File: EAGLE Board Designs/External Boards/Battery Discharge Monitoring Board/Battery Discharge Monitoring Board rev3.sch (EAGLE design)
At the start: 88 parts, among them Q1 LMMBT3904LT3G, Q2 LMMBT3904LT3G, Q3 LMMBT3904LT3G, Q4 LMMBT3904LT3G

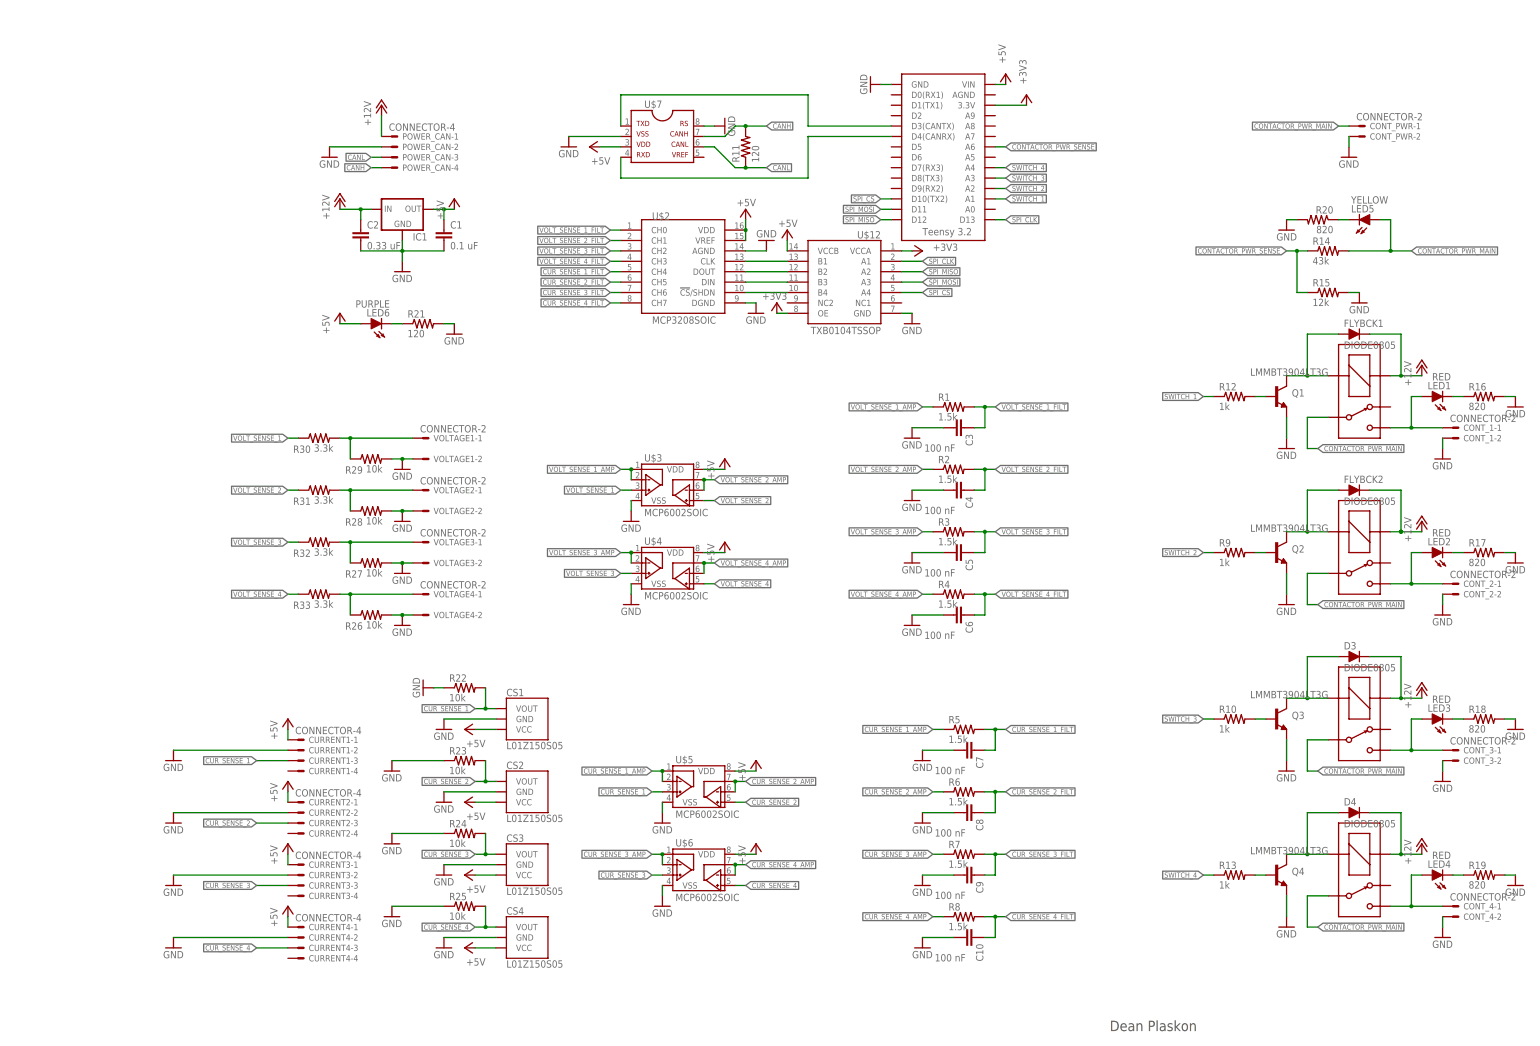
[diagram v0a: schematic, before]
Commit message: updated battery discharge monitoring rev3
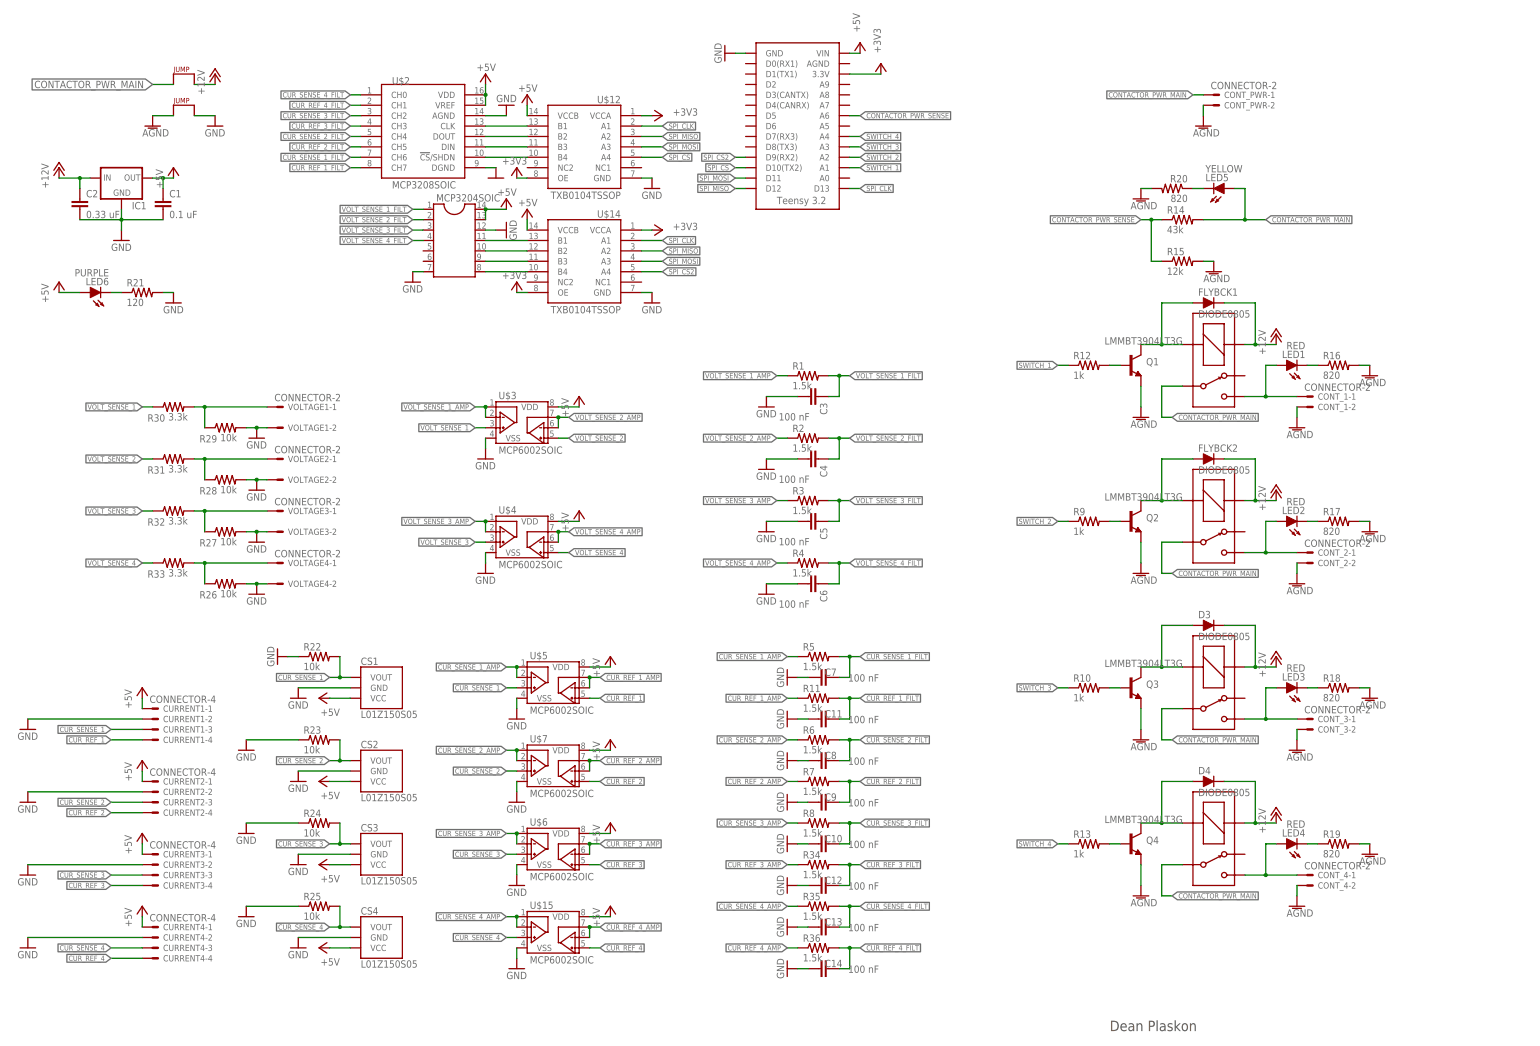
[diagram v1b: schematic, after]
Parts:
- removed POWER_CAN: CONNECTOR-4, HyTechDevices:CONNECTOR-4
- added C11, C12, C13, C14: 100 nF, HyTechDevices:CAP0805
- added J1: JUMPER.1, HyTechDevices:JUMPER.1
- added J2: JUMPER, HyTechDevices:JUMPER
- added MCP3204SOIC: (no value), MCP3204SOIC:MCP3204SOIC
- added R34, R35, R36: 1.5k, HyTechDevices:RESISTOR0805-RES
- added U$14: TXB0104TSSOP, HyTechDevices:TXB0104TSSOP
- added U$15: MCP6002SOIC, HyTechDevices:MCP6002SOIC
- R11: value 120 -> 1.5k
- U$7: value MCP2551 -> MCP6002SOIC; device HyTechDevices:MCP2551 -> HyTechDevices:MCP6002SOIC
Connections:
- removed net CANH: POWER_CAN-4.S, R11.2, U$7.7
- removed net CANL: POWER_CAN-3.S, R11.1, U$7.6
- new net AGND: CONT_1-2.S, CONT_2-2.S, CONT_3-2.S, CONT_4-2.S, CONT_PWR-2.S, J2.P$1, Q1.EMITTER, Q2.EMITTER, Q3.EMITTER, Q4.EMITTER, R15.2, R16.2, R17.2, R18.2, R19.2, R20.2
- new net CUR_REF_1: CURRENT1-4.S, U$5.VINB+
- new net CUR_REF_1_AMP: R11.1, U$5.VINB-, U$5.VOUTB
- new net CUR_REF_1_FILT: C11.1, R11.2, U$2.CH7
- new net CUR_REF_2: CURRENT2-4.S, U$7.VINB+
- new net CUR_REF_2_AMP: R7.1, U$7.VINB-, U$7.VOUTB
- new net CUR_REF_2_FILT: C9.1, R7.2, U$2.CH5
- new net CUR_REF_3: CURRENT3-4.S, U$6.VINB+
- new net CUR_REF_3_AMP: R34.1, U$6.VINB-, U$6.VOUTB
- new net CUR_REF_3_FILT: C12.1, R34.2, U$2.CH3
- new net CUR_REF_4: CURRENT4-4.S, U$15.VINB+
- new net CUR_REF_4_AMP: R36.1, U$15.VINB-, U$15.VOUTB
- new net CUR_REF_4_FILT: C14.1, R36.2, U$2.CH1
- new net N$25: MCP3204SOIC.DIN, U$14.B3
- new net N$26: MCP3204SOIC./CS, U$14.B4
- new net SPI_CS2: U$1.D9(RX2), U$14.A4
- net +12V: now also J1.P$2; no longer POWER_CAN-1.S
- net +3V3: now also U$14.OE, U$14.VCCA
- net +5V: now also MCP3204SOIC.VDD, MCP3204SOIC.VREF, U$14.VCCB, U$15.VDD, U$7.VDD; no longer U$7.3
- net CONTACTOR_PWR_MAIN: now also J1.P$1
- net CUR_SENSE_1_FILT: now also U$2.CH6; no longer U$2.CH4
- net CUR_SENSE_2: now also U$7.VINA+; no longer U$5.VINB+
- net CUR_SENSE_2_AMP: now also U$7.VINA-, U$7.VOUTA; no longer U$5.VINB-, U$5.VOUTB
- net CUR_SENSE_2_FILT: now also U$2.CH4; no longer U$2.CH5
- net CUR_SENSE_3_AMP: now also R8.1; no longer R7.1
- net CUR_SENSE_3_FILT: now also C10.1, R8.2, U$2.CH2; no longer C9.1, R7.2, U$2.CH6
- net CUR_SENSE_4: now also U$15.VINA+; no longer U$6.VINB+
- net CUR_SENSE_4_AMP: now also R35.1, U$15.VINA-, U$15.VOUTA; no longer R8.1, U$6.VINB-, U$6.VOUTB
- net CUR_SENSE_4_FILT: now also C13.1, R35.2, U$2.CH0; no longer C10.1, R8.2, U$2.CH7
- net GND: now also C11.2, C12.2, C13.2, C14.2, J2.P$2, MCP3204SOIC.AGND, MCP3204SOIC.DGND, U$14.GND, U$15.VSS, U$7.VSS; no longer CONT_1-2.S, CONT_2-2.S, CONT_3-2.S, CONT_4-2.S, CONT_PWR-2.S, POWER_CAN-2.S, Q1.EMITTER, Q2.EMITTER, Q3.EMITTER, Q4.EMITTER, R15.2, R16.2, R17.2, R18.2, R19.2, R20.2, U$7.2, U$7.8
- net N$1: now also MCP3204SOIC.CLK, U$14.B1; no longer U$1.D3(CANTX), U$7.1
- net N$2: now also MCP3204SOIC.DOUT, U$14.B2; no longer U$1.D4(CANRX), U$7.4
- net SPI_CLK: now also U$14.A1
- net SPI_MISO: now also U$14.A2
- net SPI_MOSI: now also U$14.A3
- net VOLT_SENSE_1_FILT: now also MCP3204SOIC.CH0; no longer U$2.CH0
- net VOLT_SENSE_2_FILT: now also MCP3204SOIC.CH1; no longer U$2.CH1
- net VOLT_SENSE_3_FILT: now also MCP3204SOIC.CH2; no longer U$2.CH2
- net VOLT_SENSE_4_FILT: now also MCP3204SOIC.CH3; no longer U$2.CH3
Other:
- moved on the sheet: C1, C10, C2, C3, C4, C5, C6, C7, C8, C9, CONT_1-1, CONT_1-2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
